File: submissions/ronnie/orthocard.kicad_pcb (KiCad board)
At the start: 2 copper layers, 41.3 x 76.2 mm, 47 parts, among them J1 Conn_01x04, J10 Conn_01x02, J11 Conn_01x02, J12 Conn_01x02, J2 Conn_01x02, J3 Conn_01x02, J4 Conn_01x02, J5 Conn_01x02, J6 Conn_01x02, J7 Conn_01x04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

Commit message: - added libraries - added pictures - added more documentation to the README.md - added credits
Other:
- board text added: "discord: @Gravitational Eddy#2263"
- board text added: "instagram: @bathoorn"
- board text added: "reddit: /u/bathoorn"
- board text added: "twitter: @bathoorn"

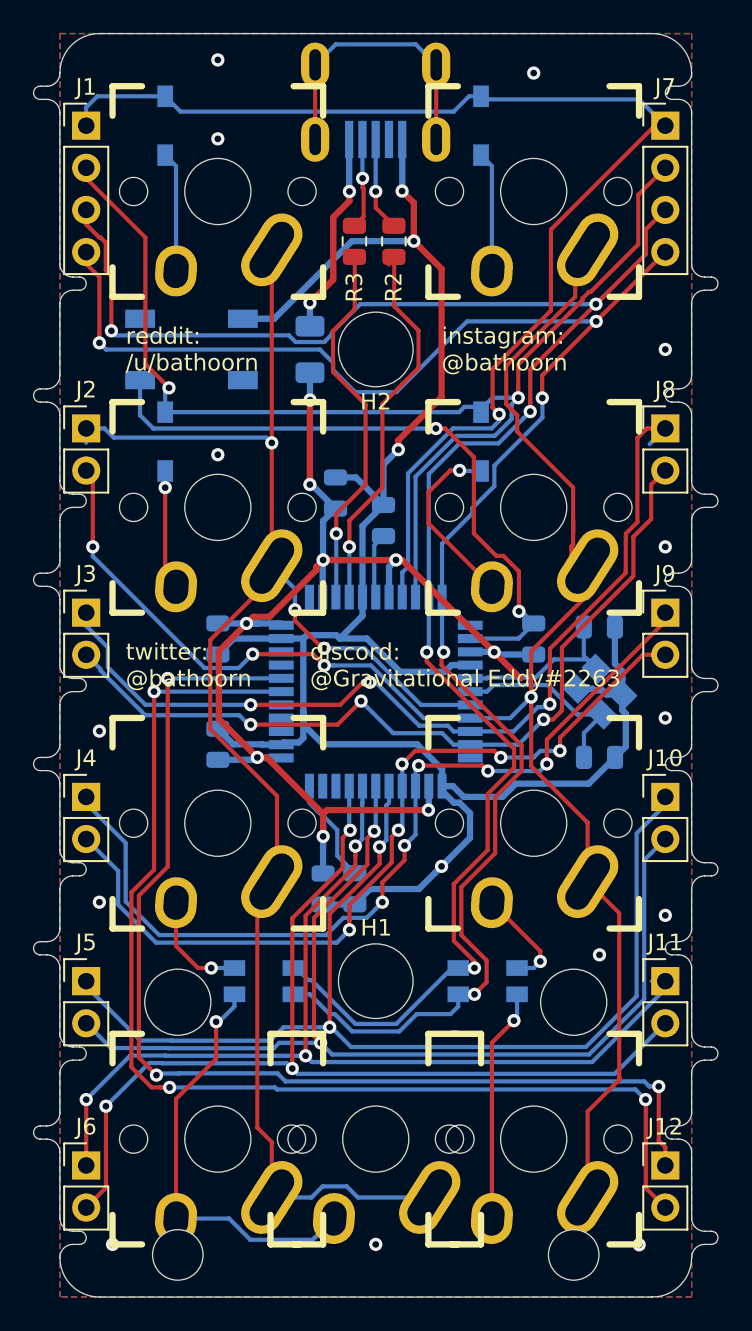
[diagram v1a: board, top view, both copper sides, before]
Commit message: made some changes based on spacemans review - added a note on the usb connector in the readme.md - created some room around a mounting hole so the traces   don't come to close - removed some hanging traces - changed the usb shield to no connect
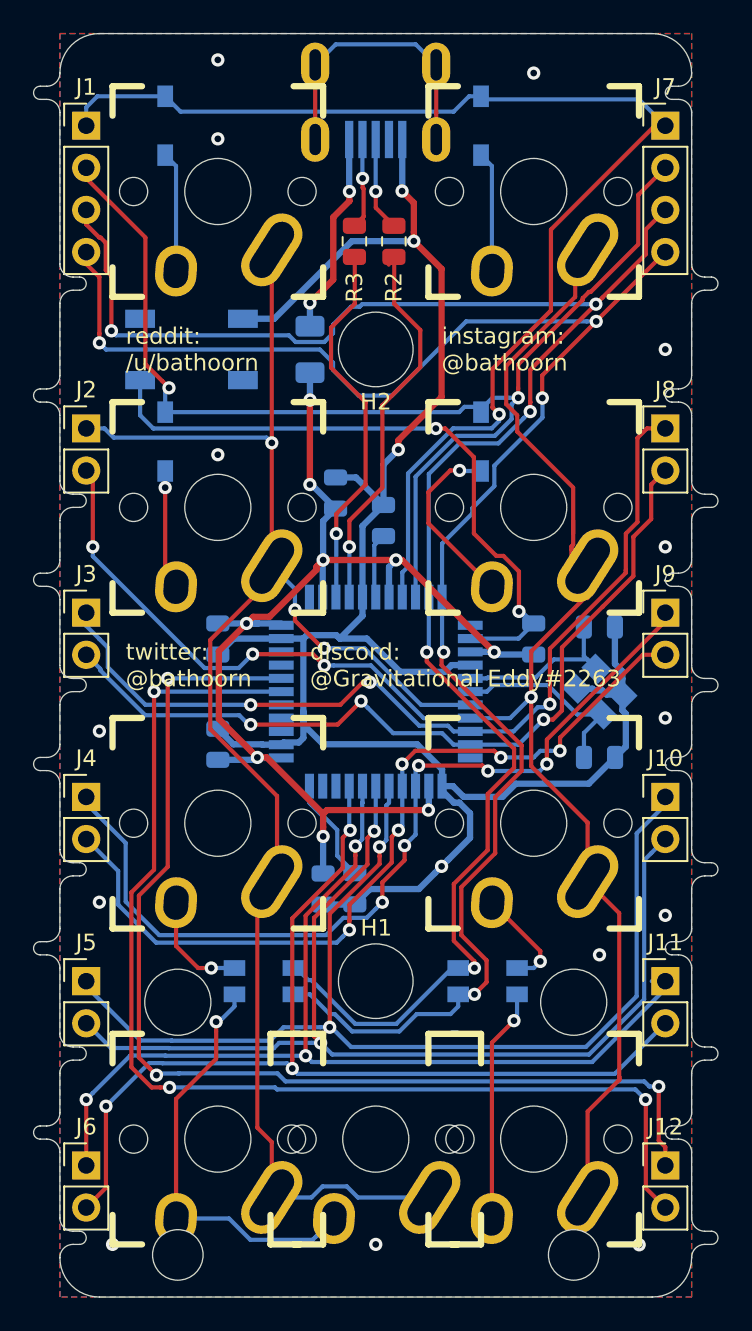
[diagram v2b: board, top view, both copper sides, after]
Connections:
- USB1 pad 6: GND -> Net-(USB1-Pad6)
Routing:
- net GND: track 144.6 -> 127.3 mm
- net Net-(USB1-Pad6): track 0.00 -> 17.3 mm
- net +5V: track 77.1 -> 74.9 mm
- net col03: track 56.2 -> 54.9 mm
- net col01: track 102.4 -> 101.5 mm
